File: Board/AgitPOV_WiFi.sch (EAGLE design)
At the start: 45 parts, among them U1 MMA8452Q

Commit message: Mean and lean board
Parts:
- removed HALL: Hall, SparkFun-Connectors:M03PTH
- removed PUSHBUTTON: (no value), switch-omron:10-XX
- removed R3: 10k, SparkFun-Resistors:RESISTOR1206
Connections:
- removed net N$41: HALL.3, WEMOS2.3
- removed net PULLDOWN: PUSHBUTTON.P, R3.2, WEMOS1.3
- removed net SA0: U1.SA0, WEMOS1.6
- net +3.3V: no longer HALL.1, PUSHBUTTON.S
- net GND: no longer HALL.2, R3.1
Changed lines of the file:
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@@
 <part name="WEMOS1" library="SparkFun-Connectors" deviceset="M08" device=""/>
 <part name="WEMOS2" library="SparkFun-Connectors" deviceset="M08" device="" value="Wemos D1 mini"/>
-<part name="HALL" library="SparkFun-Connectors" deviceset="M03" device="PTH" value="Hall"/>
 <part name="PIN0" library="SparkFun-Connectors" deviceset="M01" device="PTH"/>
 <part name="KK" library="SparkFun-Connectors" deviceset="M01" device="PTH"/>
@@
 <part name="C1" library="SparkFun-Capacitors" deviceset="10UF-16V-10%(TANT)" device="" value="0.1uF"/>
 <part name="JST" library="con-garry" deviceset="332-02" device=""/>
-<part name="PUSHBUTTON" library="switch-omron" deviceset="10-XX" device=""/>
 <part name="JP-GND" library="SparkFun-Connectors" deviceset="M01" device="PTH" value="SWITCH"/>
 <part name="JP-GNDE" library="SparkFun-Connectors" deviceset="M01" device="PTH" value="-"/>
-<part name="R3" library="SparkFun-Resistors" deviceset="RESISTOR" device="1206" value="10k"/>
 <part name="C2" library="SparkFun-Capacitors" deviceset="10UF-16V-10%(TANT)" device="" value="0.1uF"/>
 <part name="U1" library="SparkFun-Sensors" deviceset="MMA8452Q" device=""/>
@@
 <instance part="WEMOS1" gate="G$1" x="43.18" y="53.34" rot="R90"/>
 <instance part="WEMOS2" gate="G$1" x="40.64" y="40.64" rot="R270"/>
-<instance part="HALL" gate="G$1" x="71.12" y="33.02" rot="R180"/>
 <instance part="PIN0" gate="G$1" x="193.04" y="38.1"/>
 <instance part="KK" gate="G$1" x="193.04" y="25.4"/>
@@
 <attribute name="NAME" x="61.722" y="17.78" size="1.524" layer="95" rot="R90"/>
 </instance>
-<instance part="PUSHBUTTON" gate="1" x="55.88" y="66.04" rot="R270"/>
 <instance part="JP-GND" gate="G$1" x="35.56" y="10.16" rot="MR90"/>
 <instance part="JP-GNDE" gate="G$1" x="78.74" y="10.16" rot="R180"/>
-<instance part="R3" gate="G$1" x="25.4" y="60.96" rot="R90"/>
 <instance part="C2" gate="G$1" x="101.6" y="40.64"/>
 <instance part="U1" gate="G$1" x="127" y="43.18"/>
@@
 <wire x1="256.54" y1="76.2" x2="279.4" y2="76.2" width="0.1524" layer="91"/>
 <wire x1="27.94" y1="76.2" x2="27.94" y2="27.94" width="0.1524" layer="91"/>
-<pinref part="HALL" gate="G$1" pin="2"/>
-<wire x1="63.5" y1="33.02" x2="60.96" y2="33.02" width="0.1524" layer="91"/>
-<wire x1="60.96" y1="33.02" x2="60.96" y2="27.94" width="0.1524" layer="91"/>
 <pinref part="WEMOS2" gate="G$1" pin="2"/>
-<wire x1="35.56" y1="27.94" x2="35.56" y2="22.86" width="0.1524" layer="91"/>
-<wire x1="60.96" y1="27.94" x2="35.56" y2="27.94" width="0.1524" layer="91"/>
 <wire x1="35.56" y1="27.94" x2="35.56" y2="35.56" width="0.1524" layer="91"/>
 <wire x1="27.94" y1="27.94" x2="35.56" y2="27.94" width="0.1524" layer="91"/>
 <pinref part="JP-GND" gate="G$1" pin="1"/>
-<wire x1="35.56" y1="17.78" x2="35.56" y2="22.86" width="0.1524" layer="91"/>
-<wire x1="35.56" y1="22.86" x2="25.4" y2="22.86" width="0.1524" layer="91"/>
-<wire x1="25.4" y1="22.86" x2="25.4" y2="55.88" width="0.1524" layer="91"/>
-<pinref part="R3" gate="G$1" pin="1"/>
+<wire x1="35.56" y1="17.78" x2="35.56" y2="27.94" width="0.1524" layer="91"/>
 <wire x1="35.56" y1="17.78" x2="81.28" y2="17.78" width="0.1524" layer="91"/>
 <wire x1="81.28" y1="17.78" x2="81.28" y2="33.02" width="0.1524" layer="91"/>
@@
 </segment>
 </net>
-<net name="PULLDOWN" class="0">
-<segment>
-<pinref part="PUSHBUTTON" gate="1" pin="P"/>
-<pinref part="R3" gate="G$1" pin="2"/>
-<pinref part="WEMOS1" gate="G$1" pin="3"/>
-<wire x1="45.72" y1="66.04" x2="25.4" y2="66.04" width="0.1524" layer="91"/>
-<wire x1="45.72" y1="58.42" x2="45.72" y2="66.04" width="0.1524" layer="91"/>
-<wire x1="45.72" y1="66.04" x2="50.8" y2="66.04" width="0.1524" layer="91"/>
-</segment>
-</net>
 <net name="ENTREEGND" class="0">
 <segment>
@@
 </segment>
 </net>
-<net name="N$41" class="0">
-<segment>
-<pinref part="HALL" gate="G$1" pin="3"/>
-<wire x1="63.5" y1="30.48" x2="66.04" y2="30.48" width="0.1524" layer="91"/>
-<wire x1="63.5" y1="30.48" x2="38.1" y2="30.48" width="0.1524" layer="91"/>
-<wire x1="38.1" y1="40.64" x2="38.1" y2="35.56" width="0.1524" layer="91"/>
-<pinref part="WEMOS2" gate="G$1" pin="3"/>
-<wire x1="38.1" y1="35.56" x2="38.1" y2="30.48" width="0.1524" layer="91"/>
-<junction x="38.1" y="35.56"/>
-</segment>
-</net>
-<net name="SA0" class="0">
-<segment>
-<pinref part="WEMOS1" gate="G$1" pin="6"/>
-<junction x="38.1" y="58.42"/>
-<wire x1="38.1" y1="58.42" x2="38.1" y2="55.88" width="0.1524" layer="91"/>
-<wire x1="38.1" y1="58.42" x2="38.1" y2="68.58" width="0.1524" layer="91"/>
-<wire x1="38.1" y1="68.58" x2="157.48" y2="68.58" width="0.1524" layer="91"/>
-<wire x1="157.48" y1="68.58" x2="157.48" y2="35.56" width="0.1524" layer="91"/>
-<pinref part="U1" gate="G$1" pin="SA0"/>
-<wire x1="157.48" y1="35.56" x2="139.7" y2="35.56" width="0.1524" layer="91"/>
-</segment>
-</net>
 <net name="BYP" class="0">
 <segment>
@@
 <pinref part="WEMOS1" gate="G$1" pin="8"/>
 <wire x1="33.02" y1="58.42" x2="33.02" y2="60.96" width="0.1524" layer="91"/>
-<wire x1="33.02" y1="60.96" x2="63.5" y2="60.96" width="0.1524" layer="91"/>
-<pinref part="HALL" gate="G$1" pin="1"/>
-<wire x1="63.5" y1="60.96" x2="63.5" y2="35.56" width="0.1524" layer="91"/>
+<wire x1="33.02" y1="60.96" x2="81.28" y2="60.96" width="0.1524" layer="91"/>
 <pinref part="R2" gate="G$1" pin="2"/>
 <pinref part="R1" gate="G$1" pin="2"/>
-<pinref part="PUSHBUTTON" gate="1" pin="S"/>
-<wire x1="60.96" y1="66.04" x2="63.5" y2="66.04" width="0.1524" layer="91"/>
-<wire x1="63.5" y1="66.04" x2="63.5" y2="60.96" width="0.1524" layer="91"/>
-<wire x1="81.28" y1="60.96" x2="63.5" y2="60.96" width="0.1524" layer="91"/>
 <pinref part="U1" gate="G$1" pin="VDD"/>
 <wire x1="81.28" y1="60.96" x2="81.28" y2="43.18" width="0.1524" layer="91"/>

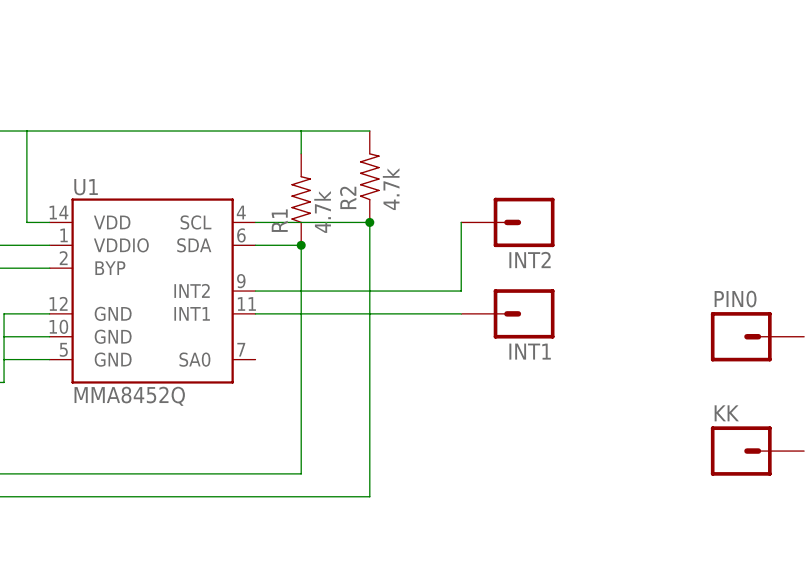
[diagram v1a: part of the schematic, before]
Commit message: New board version, FastLED display works.
Board : removed button, Hall sensor, back to smd switch, cleaning
around the accelerometer, removed int1 + int2, one less via! More space
for the LEDs -> resized board.
FastLED : correct GRB color space, bizarro world to display text on
both sides.
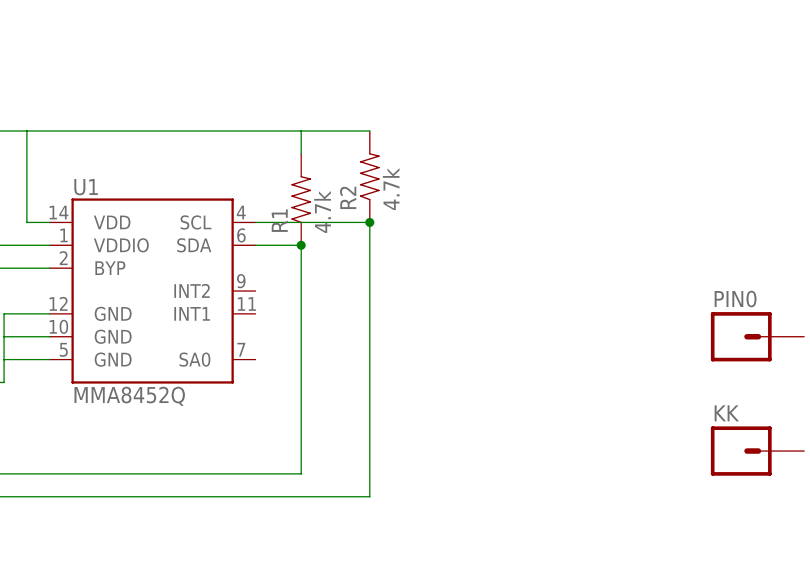
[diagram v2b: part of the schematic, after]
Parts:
- removed INT1, INT2: (no value), SparkFun-Connectors:M01PTH
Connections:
- removed net N$65: INT1.1, U1.INT1
- removed net N$67: INT2.1, U1.INT2
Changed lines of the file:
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@@
 <part name="U1" library="SparkFun-Sensors" deviceset="MMA8452Q" device=""/>
 <part name="C3" library="SparkFun-Capacitors" deviceset="10UF-16V-10%(TANT)" device="" value="4.7uF"/>
-<part name="INT1" library="SparkFun-Connectors" deviceset="M01" device="PTH"/>
-<part name="INT2" library="SparkFun-Connectors" deviceset="M01" device="PTH"/>
 </parts>
 <sheets>
@@
 <instance part="U1" gate="G$1" x="127" y="43.18"/>
 <instance part="C3" gate="G$1" x="81.28" y="40.64"/>
-<instance part="INT1" gate="G$1" x="170.18" y="40.64" rot="R180"/>
-<instance part="INT2" gate="G$1" x="170.18" y="50.8" rot="R180"/>
 </instances>
 <busses>
@@
 </segment>
 </net>
-<net name="N$65" class="0">
-<segment>
-<pinref part="U1" gate="G$1" pin="INT1"/>
-<pinref part="INT1" gate="G$1" pin="1"/>
-<wire x1="139.7" y1="40.64" x2="162.56" y2="40.64" width="0.1524" layer="91"/>
-</segment>
-</net>
-<net name="N$67" class="0">
-<segment>
-<pinref part="U1" gate="G$1" pin="INT2"/>
-<pinref part="INT2" gate="G$1" pin="1"/>
-<wire x1="139.7" y1="43.18" x2="162.56" y2="43.18" width="0.1524" layer="91"/>
-<wire x1="162.56" y1="43.18" x2="162.56" y2="50.8" width="0.1524" layer="91"/>
-</segment>
-</net>
